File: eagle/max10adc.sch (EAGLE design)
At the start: 203 parts, among them IC1 MAX19506, IC2 MAX19506, J1 MOLEX_BNC_73100-0105, J2 MOLEX_BNC_73100-0105, J3 MOLEX_BNC_73100-0105, J4 MOLEX_BNC_73100-0105, K1 AQY21SOP, K2 AQY21SOP, K3 AQY21SOP, K4 AQY21SOP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

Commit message: for 8.7 and USB2
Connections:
- net +3V3: no longer PIN_DISPLAY.2
- net +5V: now also PIN_DISPLAY.2
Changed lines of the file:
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@@
 <part name="USB1" library="PP_Connectors" deviceset="USB_5PIN" device="_10118193-0001LF" value="MF-CON-MICROUSB-RIGHT"/>
 <part name="GND42" library="supply1" deviceset="GND" device=""/>
-<part name="+3V22" library="supply1" deviceset="+3V3" device=""/>
 <part name="SW_RESET" library="MF_Switches" deviceset="TACT" device="_4.2MM" value="MF-SW-TACT-4.2MM"/>
 <part name="+3V16" library="supply1" deviceset="+3V3" device=""/>
@@
 <attribute name="MPN" value="MF-CAP-0805-1uF"/>
 </part>
+<part name="P+6" library="supply1" deviceset="+5V" device=""/>
 </parts>
 <sheets>
@@
 <instance part="USB1" gate="G$1" x="-375.92" y="-104.14"/>
 <instance part="GND42" gate="1" x="-480.06" y="78.994"/>
-<instance part="+3V22" gate="G$1" x="-474.98" y="68.58" smashed="yes" rot="R180">
-<attribute name="VALUE" x="-474.98" y="72.39" size="1.778" layer="96" rot="R90"/>
-</instance>
 <instance part="SW_RESET" gate="G$1" x="-431.8" y="86.36" smashed="yes">
 <attribute name="NAME" x="-434.34" y="86.36" size="1.016" layer="95" font="vector" align="top-left"/>
@@
 <attribute name="NAME" x="-461.01" y="111.76" size="1.27" layer="95" ratio="10" rot="R180"/>
 </instance>
-<instance part="P+7" gate="1" x="-474.98" y="121.92"/>
-<instance part="GND68" gate="1" x="-477.52" y="114.3" rot="R180"/>
+<instance part="P+7" gate="1" x="-480.06" y="96.52" rot="R90"/>
+<instance part="GND68" gate="1" x="-480.06" y="101.6"/>
 <instance part="GND69" gate="1" x="-355.6" y="-116.84" rot="R90"/>
 <instance part="K1" gate="G$1" x="-228.6" y="-104.14" rot="R180"/>
@@
 <attribute name="MPN" x="-596.9" y="-60.96" size="1.778" layer="96" display="off"/>
 </instance>
+<instance part="P+6" gate="1" x="-480.06" y="73.66" rot="R90"/>
 </instances>
 <busses>
@@
 <pinref part="PIN_IO_1" gate="G$1" pin="2"/>
 <pinref part="P+7" gate="1" pin="+5V"/>
-<wire x1="-474.98" y1="119.38" x2="-474.98" y2="104.14" width="0.1524" layer="91"/>
+<wire x1="-477.52" y1="96.52" x2="-474.98" y2="104.14" width="0.1524" layer="91"/>
 </segment>
 <segment>
@@
 <pinref part="P+4" gate="1" pin="+5V"/>
 <wire x1="-337.82" y1="-127" x2="-337.82" y2="-121.92" width="0.1524" layer="91"/>
+</segment>
+<segment>
+<pinref part="PIN_DISPLAY" gate="G$1" pin="2"/>
+<wire x1="-477.52" y1="73.66" x2="-474.98" y2="81.534" width="0.1524" layer="91"/>
+<pinref part="P+6" gate="1" pin="+5V"/>
 </segment>
 </net>
@@
 <pinref part="PIN_IO_1" gate="G$1" pin="1"/>
 <pinref part="GND68" gate="1" pin="GND"/>
-<wire x1="-477.52" y1="111.76" x2="-477.52" y2="104.14" width="0.1524" layer="91"/>
+<wire x1="-480.06" y1="104.14" x2="-477.52" y2="104.14" width="0.1524" layer="91"/>
 </segment>
 <segment>
@@
 <junction x="-393.7" y="-142.24"/>
 </segment>
-<segment>
-<pinref part="+3V22" gate="G$1" pin="+3V3"/>
-<pinref part="PIN_DISPLAY" gate="G$1" pin="2"/>
-<wire x1="-474.98" y1="71.12" x2="-474.98" y2="81.534" width="0.1524" layer="91"/>
-</segment>
 </net>

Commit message: for 8.7 use 1210 10uF caps for offset
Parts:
- removed COFFSETB11, COFFSETB5, COFFSETB7, COFFSETB9: 10uF, rcl:C-EUC0805K
- added COFFSETA1, COFFSETA2, COFFSETA3, COFFSETA6: 10uF, rcl@1:C-USC1206
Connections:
- net GND: now also COFFSETA1.1, COFFSETA2.1, COFFSETA3.1, COFFSETA6.1; no longer COFFSETB11.1, COFFSETB5.1, COFFSETB7.1, COFFSETB9.1
- net OFFSET1: now also COFFSETA6.2; no longer COFFSETB5.2
- net OFFSET2: now also COFFSETA1.2; no longer COFFSETB7.2
- net OFFSET3: now also COFFSETA2.2; no longer COFFSETB9.2
- net OFFSET4: now also COFFSETA3.2; no longer COFFSETB11.2
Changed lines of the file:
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@@
 <part name="GND60" library="supply1" deviceset="GND" device=""/>
 <part name="GND61" library="supply1" deviceset="GND" device=""/>
-<part name="COFFSETB5" library="rcl" deviceset="C-EU" device="C0805K" value="10uF">
-<attribute name="MPN" value="MF-CAP-0805-10uF"/>
-</part>
 <part name="COFFSETB6" library="rcl" deviceset="C-EU" device="C0805K" value="0.1uF">
 <attribute name="MPN" value="MF-CAP-0805-0.1uF"/>
 </part>
 <part name="GND58" library="supply1" deviceset="GND" device=""/>
-<part name="COFFSETB7" library="rcl" deviceset="C-EU" device="C0805K" value="10uF">
-<attribute name="MPN" value="MF-CAP-0805-10uF"/>
-</part>
 <part name="COFFSETB8" library="rcl" deviceset="C-EU" device="C0805K" value="0.1uF">
 <attribute name="MPN" value="MF-CAP-0805-0.1uF"/>
 </part>
 <part name="GND59" library="supply1" deviceset="GND" device=""/>
-<part name="COFFSETB9" library="rcl" deviceset="C-EU" device="C0805K" value="10uF">
-<attribute name="MPN" value="MF-CAP-0805-10uF"/>
-</part>
 <part name="COFFSETB10" library="rcl" deviceset="C-EU" device="C0805K" value="0.1uF">
 <attribute name="MPN" value="MF-CAP-0805-0.1uF"/>
 </part>
 <part name="GND62" library="supply1" deviceset="GND" device=""/>
-<part name="COFFSETB11" library="rcl" deviceset="C-EU" device="C0805K" value="10uF">
-<attribute name="MPN" value="MF-CAP-0805-10uF"/>
-</part>
 <part name="COFFSETB12" library="rcl" deviceset="C-EU" device="C0805K" value="0.1uF">
 <attribute name="MPN" value="MF-CAP-0805-0.1uF"/>
@@
 </part>
 <part name="P+6" library="supply1" deviceset="+5V" device=""/>
+<part name="COFFSETA6" library="rcl@1" deviceset="C-US" device="C1206" value="10uF">
+<attribute name="MPN" value="MF-CAP-1206-10uF"/>
+</part>
+<part name="COFFSETA1" library="rcl@1" deviceset="C-US" device="C1206" value="10uF">
+<attribute name="MPN" value="MF-CAP-1206-10uF"/>
+</part>
+<part name="COFFSETA2" library="rcl@1" deviceset="C-US" device="C1206" value="10uF">
+<attribute name="MPN" value="MF-CAP-1206-10uF"/>
+</part>
+<part name="COFFSETA3" library="rcl@1" deviceset="C-US" device="C1206" value="10uF">
+<attribute name="MPN" value="MF-CAP-1206-10uF"/>
+</part>
 </parts>
 <sheets>
@@
 <instance part="GND60" gate="1" x="-96.52" y="30.48"/>
 <instance part="GND61" gate="1" x="-96.52" y="53.34"/>
-<instance part="COFFSETB5" gate="G$1" x="-254" y="-215.9" smashed="yes" rot="R180">
-<attribute name="MPN" x="-254" y="-215.9" size="1.778" layer="96" rot="R180" display="off"/>
-<attribute name="NAME" x="-250.444" y="-221.361" size="1.778" layer="95" rot="R180"/>
-<attribute name="VALUE" x="-255.524" y="-211.201" size="1.778" layer="96" rot="R180"/>
-</instance>
 <instance part="COFFSETB6" gate="G$1" x="-261.62" y="-215.9" smashed="yes" rot="R180">
 <attribute name="MPN" x="-261.62" y="-215.9" size="1.778" layer="96" rot="R180" display="off"/>
@@
 </instance>
 <instance part="GND58" gate="1" x="-254" y="-223.52"/>
-<instance part="COFFSETB7" gate="G$1" x="-182.88" y="-218.44" smashed="yes" rot="R180">
-<attribute name="MPN" x="-182.88" y="-218.44" size="1.778" layer="96" rot="R180" display="off"/>
-<attribute name="NAME" x="-179.324" y="-223.901" size="1.778" layer="95" rot="R180"/>
-<attribute name="VALUE" x="-184.404" y="-213.741" size="1.778" layer="96" rot="R180"/>
-</instance>
 <instance part="COFFSETB8" gate="G$1" x="-190.5" y="-218.44" smashed="yes" rot="R180">
 <attribute name="MPN" x="-190.5" y="-218.44" size="1.778" layer="96" rot="R180" display="off"/>
@@
 </instance>
 <instance part="GND59" gate="1" x="-182.88" y="-226.06"/>
-<instance part="COFFSETB9" gate="G$1" x="-170.18" y="-215.9" smashed="yes" rot="R180">
-<attribute name="MPN" x="-170.18" y="-215.9" size="1.778" layer="96" rot="R180" display="off"/>
-<attribute name="NAME" x="-166.624" y="-221.361" size="1.778" layer="95" rot="R180"/>
-<attribute name="VALUE" x="-171.704" y="-211.201" size="1.778" layer="96" rot="R180"/>
-</instance>
 <instance part="COFFSETB10" gate="G$1" x="-177.8" y="-215.9" smashed="yes" rot="R180">
 <attribute name="MPN" x="-177.8" y="-215.9" size="1.778" layer="96" rot="R180" display="off"/>
@@
 </instance>
 <instance part="GND62" gate="1" x="-170.18" y="-223.52"/>
-<instance part="COFFSETB11" gate="G$1" x="-96.52" y="-218.44" smashed="yes" rot="R180">
-<attribute name="MPN" x="-96.52" y="-218.44" size="1.778" layer="96" rot="R180" display="off"/>
-<attribute name="NAME" x="-92.964" y="-223.901" size="1.778" layer="95" rot="R180"/>
-<attribute name="VALUE" x="-98.044" y="-213.741" size="1.778" layer="96" rot="R180"/>
-</instance>
 <instance part="COFFSETB12" gate="G$1" x="-104.14" y="-218.44" smashed="yes" rot="R180">
 <attribute name="MPN" x="-104.14" y="-218.44" size="1.778" layer="96" rot="R180" display="off"/>
@@
 </instance>
 <instance part="P+6" gate="1" x="-480.06" y="73.66" rot="R90"/>
+<instance part="COFFSETA6" gate="G$1" x="-254" y="-215.9" rot="R180">
+<attribute name="MPN" x="-254" y="-215.9" size="1.778" layer="96" rot="R180" display="off"/>
+</instance>
+<instance part="COFFSETA1" gate="G$1" x="-182.88" y="-218.44" rot="R180">
+<attribute name="MPN" x="-182.88" y="-218.44" size="1.778" layer="96" rot="R180" display="off"/>
+</instance>
+<instance part="COFFSETA2" gate="G$1" x="-170.18" y="-215.9" rot="R180">
+<attribute name="MPN" x="-170.18" y="-215.9" size="1.778" layer="96" rot="R180" display="off"/>
+</instance>
+<instance part="COFFSETA3" gate="G$1" x="-96.52" y="-218.44" rot="R180">
+<attribute name="MPN" x="-96.52" y="-218.44" size="1.778" layer="96" rot="R180" display="off"/>
+</instance>
 </instances>
 <busses>
@@
 </segment>
 <segment>
-<pinref part="COFFSETB5" gate="G$1" pin="1"/>
 <pinref part="GND58" gate="1" pin="GND"/>
 <wire x1="-254" y1="-220.98" x2="-254" y2="-218.44" width="0.1524" layer="91"/>
 <pinref part="COFFSETB6" gate="G$1" pin="1"/>
 <wire x1="-261.62" y1="-218.44" x2="-254" y2="-218.44" width="0.1524" layer="91"/>
+<pinref part="COFFSETA6" gate="G$1" pin="1"/>
 <junction x="-254" y="-218.44"/>
 </segment>
 <segment>
-<pinref part="COFFSETB7" gate="G$1" pin="1"/>
 <pinref part="GND59" gate="1" pin="GND"/>
 <wire x1="-182.88" y1="-223.52" x2="-182.88" y2="-220.98" width="0.1524" layer="91"/>
 <pinref part="COFFSETB8" gate="G$1" pin="1"/>
 <wire x1="-190.5" y1="-220.98" x2="-182.88" y2="-220.98" width="0.1524" layer="91"/>
+<pinref part="COFFSETA1" gate="G$1" pin="1"/>
 <junction x="-182.88" y="-220.98"/>
 </segment>
 <segment>
-<pinref part="COFFSETB9" gate="G$1" pin="1"/>
 <pinref part="GND62" gate="1" pin="GND"/>
 <wire x1="-170.18" y1="-220.98" x2="-170.18" y2="-218.44" width="0.1524" layer="91"/>
 <pinref part="COFFSETB10" gate="G$1" pin="1"/>
 <wire x1="-177.8" y1="-218.44" x2="-170.18" y2="-218.44" width="0.1524" layer="91"/>
+<pinref part="COFFSETA2" gate="G$1" pin="1"/>
 <junction x="-170.18" y="-218.44"/>
 </segment>
 <segment>
-<pinref part="COFFSETB11" gate="G$1" pin="1"/>
 <pinref part="GND63" gate="1" pin="GND"/>
 <wire x1="-96.52" y1="-223.52" x2="-96.52" y2="-220.98" width="0.1524" layer="91"/>
 <pinref part="COFFSETB12" gate="G$1" pin="1"/>
 <wire x1="-104.14" y1="-220.98" x2="-96.52" y2="-220.98" width="0.1524" layer="91"/>
+<pinref part="COFFSETA3" gate="G$1" pin="1"/>
 <junction x="-96.52" y="-220.98"/>
 </segment>
@@
 <net name="OFFSET1" class="0">
 <segment>
-<wire x1="-246.38" y1="-210.82" x2="-254" y2="-210.82" width="0.1524" layer="91"/>
 <label x="-264.16" y="-210.82" size="1.778" layer="95"/>
 <pinref part="U1" gate="A" pin="+INA"/>
-<pinref part="COFFSETB5" gate="G$1" pin="2"/>
-<wire x1="-254" y1="-210.82" x2="-261.62" y2="-210.82" width="0.1524" layer="91"/>
-<junction x="-254" y="-210.82"/>
+<wire x1="-246.38" y1="-210.82" x2="-254" y2="-210.82" width="0.1524" layer="91"/>
 <pinref part="COFFSETB6" gate="G$1" pin="2"/>
 <junction x="-261.62" y="-210.82"/>
+<wire x1="-254" y1="-210.82" x2="-261.62" y2="-210.82" width="0.1524" layer="91"/>
 <wire x1="-261.62" y1="-210.82" x2="-264.16" y2="-210.82" width="0.1524" layer="91"/>
+<pinref part="COFFSETA6" gate="G$1" pin="2"/>
+<junction x="-254" y="-210.82"/>
 </segment>
 <segment>
@@
 <wire x1="-190.5" y1="-213.36" x2="-182.88" y2="-213.36" width="0.1524" layer="91"/>
 <label x="-193.04" y="-213.36" size="1.778" layer="95"/>
-<pinref part="COFFSETB7" gate="G$1" pin="2"/>
 <pinref part="COFFSETB8" gate="G$1" pin="2"/>
 <junction x="-190.5" y="-213.36"/>
-<junction x="-182.88" y="-213.36"/>
+<pinref part="COFFSETA1" gate="G$1" pin="2"/>
 <wire x1="-182.88" y1="-213.36" x2="-180.34" y2="-213.36" width="0.1524" layer="91"/>
+<junction x="-182.88" y="-213.36"/>
 </segment>
 <segment>
@@
 <segment>
 <pinref part="U2" gate="A" pin="+INA"/>
-<wire x1="-165.1" y1="-210.82" x2="-170.18" y2="-210.82" width="0.1524" layer="91"/>
 <label x="-182.88" y="-210.82" size="1.778" layer="95"/>
 <pinref part="COFFSETB10" gate="G$1" pin="2"/>
 <junction x="-177.8" y="-210.82"/>
+<wire x1="-165.1" y1="-210.82" x2="-170.18" y2="-210.82" width="0.1524" layer="91"/>
 <wire x1="-170.18" y1="-210.82" x2="-177.8" y2="-210.82" width="0.1524" layer="91"/>
 <wire x1="-177.8" y1="-210.82" x2="-182.88" y2="-210.82" width="0.1524" layer="91"/>
-<pinref part="COFFSETB9" gate="G$1" pin="2"/>
+<pinref part="COFFSETA2" gate="G$1" pin="2"/>
 <junction x="-170.18" y="-210.82"/>
 </segment>
@@
 <junction x="-104.14" y="-213.36"/>
 <wire x1="-104.14" y1="-213.36" x2="-96.52" y2="-213.36" width="0.1524" layer="91"/>
-<pinref part="COFFSETB11" gate="G$1" pin="2"/>
-<junction x="-96.52" y="-213.36"/>
+<pinref part="COFFSETA3" gate="G$1" pin="2"/>
 <wire x1="-96.52" y1="-213.36" x2="-93.98" y2="-213.36" width="0.1524" layer="91"/>
+<junction x="-96.52" y="-213.36"/>
 </segment>
 <segment>

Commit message: v8.7 just ordered from AllPCB
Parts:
- removed CIN1, CIN2, CIN3, CIN4: 10pF, rcl@1:C-USC0603
- removed CIN56_5, CIN56_6, CIN56_7, CIN56_8: 56pF, rcl@1:C-USC0603
- removed HGR1, HGR2, HGR3, HGR4: 560, resistor:R-EU_R0805
- removed K5, K6, K7, K8: AQY21SOP, relay:AQY21SOP
- added C1, C2, C3, C4: 3-10pF, SparkFun-Passives:CAP_ADJSMD
- added CIN5_1, CIN5_2, CIN5_3, CIN5_4: 5pF, rcl@1:C-USC0603
- added C_S1, C_S2, C_S3, C_S4: 8-45pF, SparkFun-Passives:CAP_ADJSMD
- added LEDPOW: MF-LED-0805-RED, led:LEDSML0805
- added RIN5, RIN6, RIN7, RIN8: 1M, resistor:R-EU_R0805
- added RLEDPOW: 560, resistor:R-EU_R0805
- added SW_SUPER1, SW_SUPER2, SW_SUPER3, SW_SUPER4: 0S102011MS2QS1, PP_Electromechanical:SPDT_0S102011MS2QS1
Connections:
- removed net E_20_B7: IOEXPAND_0X20_BOT.GPB7, PIN_AIN_IO2_PWRGND.2
- removed net E_HIGHGAIN1: HGR1.1, IOEXPAND_0X20_BOT.GPA4
- removed net E_HIGHGAIN2: HGR2.1, IOEXPAND_0X20_BOT.GPA5
- removed net E_HIGHGAIN3: HGR3.1, IOEXPAND_0X20_BOT.GPA6
- removed net E_HIGHGAIN4: HGR4.1, IOEXPAND_0X20_BOT.GPA7
- removed net E_SHDN: IC1.SHDN, IC2.SHDN, IOEXPAND_0X20_BOT.GPB4
- removed net N$36: HGR2.2, K6.A
- removed net N$37: HGR3.2, K7.A
- removed net N$43: HGR4.2, K8.A
- new net E_SHDN1: IC1.SHDN, IOEXPAND_0X20_BOT.GPB4
- new net E_SHDN2: IC2.SHDN, IOEXPAND_0X20_BOT.GPB5
- net +3V3: now also LEDPOW.A, PIN_AIN_IO2_PWRGND.3
- net AIN1: now also PIN_AIN_IO2_PWRGND.2; no longer PIN_AIN_IO2_PWRGND.1
- net E_OVSAMP1: now also IOEXPAND_0X20_BOT.GPA4; no longer IOEXPAND_0X20_BOT.GPB5
- net E_OVSAMP2: now also IOEXPAND_0X20_BOT.GPA5; no longer IOEXPAND_0X20_BOT.GPB6
- net GND: now also PIN_AIN_IO2_PWRGND.1, RIN5.2, RIN6.2, RIN7.2, RIN8.2, RLEDPOW.2; no longer K5.K, K6.K, K7.K, K8.K, PIN_AIN_IO2_PWRGND.4
- net INAMINUS1: now also C1.4, CIN5_1.1, C_S1.4; no longer CIN1.2, CIN56_2.2
- net INAMINUS2: now also C3.4, CIN56_3.2, CIN5_3.1, C_S3.4; no longer CIN3.2, CIN56_5.2, CIN56_6.2
- net INBMINUS1: now also C2.4, CIN56_2.2, CIN5_2.1, C_S2.4; no longer CIN2.2, CIN56_3.2, CIN56_4.2
- net INBMINUS2: now also C4.4, CIN56_4.2, CIN5_4.1, C_S4.4; no longer CIN4.2, CIN56_7.2, CIN56_8.2
- net IO_100: now also PIN_AIN_IO2_PWRGND.13; no longer PIN_AIN_IO2_PWRGND.11
- net IO_101: now also PIN_AIN_IO2_PWRGND.15; no longer PIN_AIN_IO2_PWRGND.13
- net IO_CLK_88: now also PIN_AIN_IO2_PWRGND.5; no longer PIN_AIN_IO2_PWRGND.3
- net IO_CLK_89: now also PIN_AIN_IO2_PWRGND.7; no longer PIN_AIN_IO2_PWRGND.5
- net IO_CLK_90: now also PIN_AIN_IO2_PWRGND.9; no longer PIN_AIN_IO2_PWRGND.7
- net IO_CLK_91: now also PIN_AIN_IO2_PWRGND.11; no longer PIN_AIN_IO2_PWRGND.9
- net L121: now also PIN_AIN_IO2_PWRGND.4; no longer PIN_AIN_IO2_PWRGND.15
- net N$10: now also C1.3, CIN5_1.2, RIN5.1, SW_SUPER1.C; no longer CIN1.1, K5.DS2
- net N$15: now also C2.3, CIN5_2.2, RIN6.1, SW_SUPER2.C; no longer CIN2.1, K6.DS2
- net N$20: now also C_S1.3, SW_SUPER1.2; no longer CIN56_2.1, K5.DS1
- net N$34: now also LEDPOW.C, RLEDPOW.1; no longer HGR1.2, K5.A
- net N$38: now also CIN56_2.1, C_S2.3, SW_SUPER2.2; no longer CIN56_3.1, CIN56_4.1, K6.DS1
- net N$39: now also C3.3, CIN5_3.2, RIN7.1, SW_SUPER3.C; no longer CIN3.1, K7.DS2
- net N$40: now also CIN56_3.1, C_S3.3, SW_SUPER3.2; no longer CIN56_5.1, CIN56_6.1, K7.DS1
- net N$41: now also C4.3, CIN5_4.2, RIN8.1, SW_SUPER4.C; no longer CIN4.1, K8.DS2
- net N$42: now also CIN56_4.1, C_S4.3, SW_SUPER4.2; no longer CIN56_7.1, CIN56_8.1, K8.DS1
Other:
- moved on the sheet: CIN56_2, CIN56_3, CIN56_4

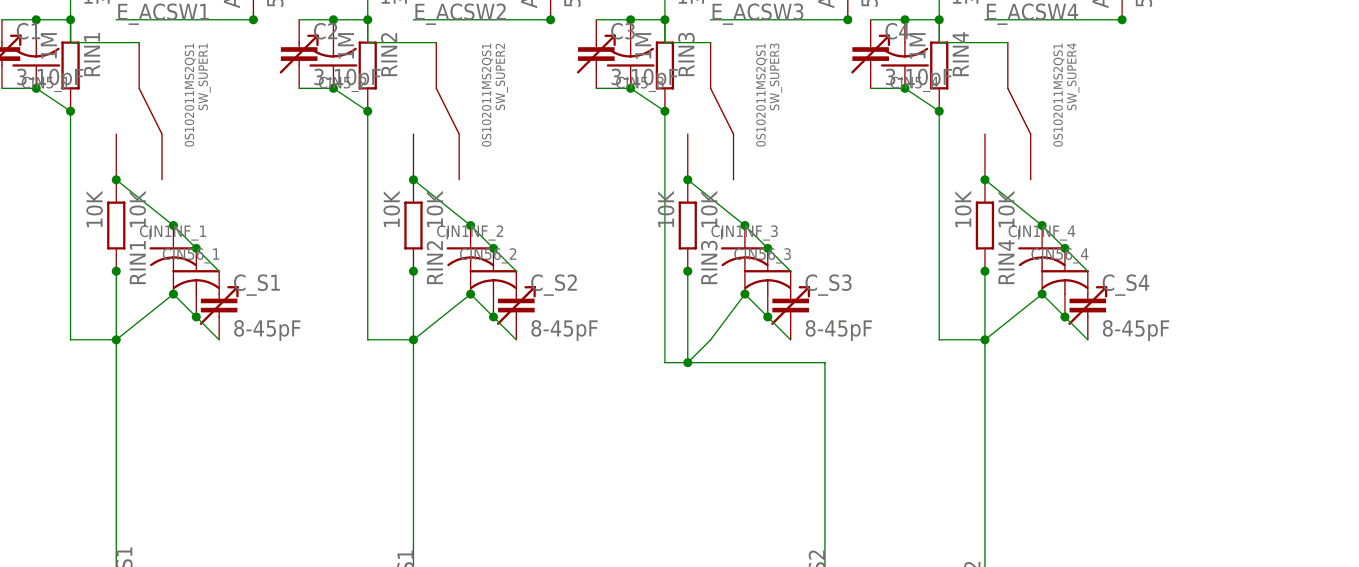
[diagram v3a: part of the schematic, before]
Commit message: v8.8 with 50pF low gain caps
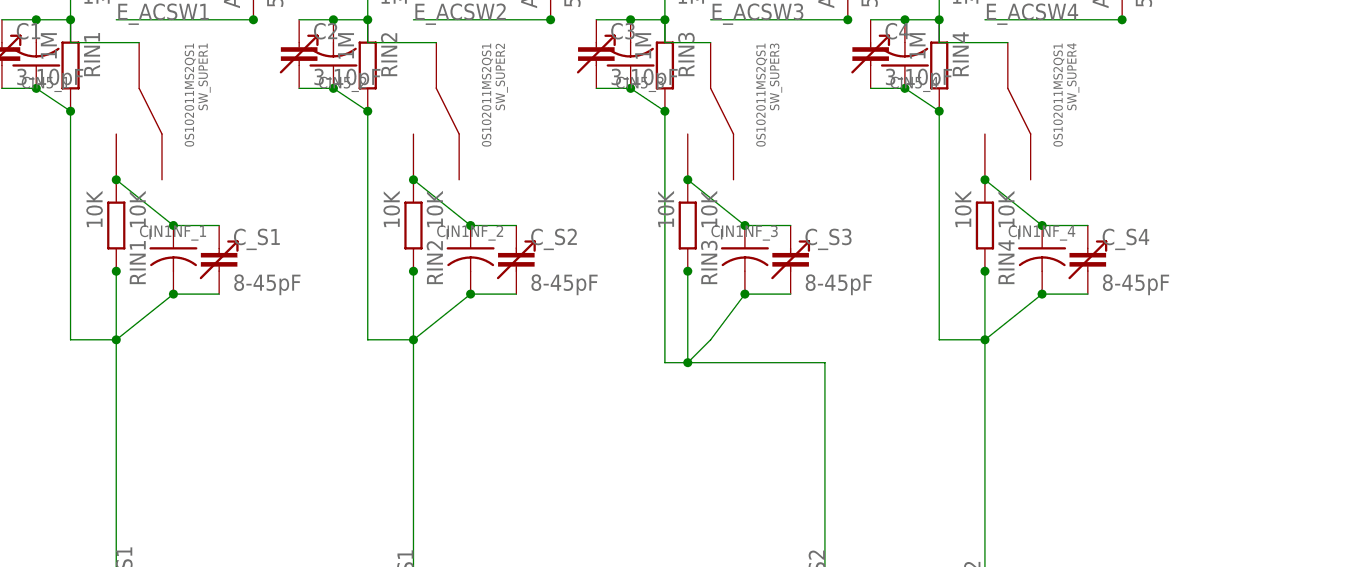
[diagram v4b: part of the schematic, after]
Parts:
- removed CIN56_1, CIN56_2, CIN56_3, CIN56_4: 56pF, rcl@1:C-USC0603
- CGAIN1_1, CGAIN1_2, CGAIN1_3, CGAIN1_4: value 56pF -> 50pF; MPN 06035A560FAT2A -> 06035A500JAT2A
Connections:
- net INAMINUS1: no longer CIN56_1.2
- net INAMINUS2: no longer CIN56_3.2
- net INBMINUS1: no longer CIN56_2.2
- net INBMINUS2: no longer CIN56_4.2
- net N$20: no longer CIN56_1.1
- net N$38: no longer CIN56_2.1
- net N$40: no longer CIN56_3.1
- net N$42: no longer CIN56_4.1
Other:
- moved on the sheet: C_S1, C_S2, C_S3, C_S4

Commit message: v8.8
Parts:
- removed C1, C2, C3, C4: 3-10pF, SparkFun-Passives:CAP_ADJSMD
- removed CGAIN2_1, CGAIN2_2, CGAIN2_3, CGAIN2_4: 5pF, rcl@1:C-USC0603
- removed C_S1, C_S2, C_S3, C_S4: 8-45pF, SparkFun-Passives:CAP_ADJSMD
- added CH1, CH2, CH3, CH4: 3-10pF, SparkFun-Passives:CAP_ADJSMD
- added CIN56_1, CIN56_2, CIN56_3, CIN56_4: 56pF, rcl@1:C-USC0603
- added CL1, CL2, CL3, CL4: 8-45pF, SparkFun-Passives:CAP_ADJSMD
- CGAIN1_1, CGAIN1_2, CGAIN1_3, CGAIN1_4: value 50pF -> 33pF; MPN 06035A500JAT2A -> 06033A330JAT2A
- CIN1NF_1, CIN1NF_2, CIN1NF_3, CIN1NF_4: MFN MF-CAP-0603-1nF -> (none); MPN (none) -> 06035A102JAT2A
- CIN5_1, CIN5_2, CIN5_3, CIN5_4: value 5pF -> 10pF; MPN C1608C0G1H050C080AA -> MF-CAP-0603-10pF
- R_SCL, R_SDA: value 4.7k -> 10K; MPN MF-RES-0805-4.7K -> MF-RES-0805-10K
- SW_5V, SW_SUPER1, SW_SUPER2, SW_SUPER3, SW_SUPER4, SW_TERM1, SW_TERM2, SW_TERM3, SW_TERM4: value 0S102011MS2QS1 -> OS102011MS2QN1
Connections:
- removed net N$42: CIN1NF_4.1, C_S4.3, RIN4_10K.1, SW_SUPER4.2
- new net N$36: CIN1NF_4.1, CIN56_4.1, RIN4_10K.1, SW_SUPER4.2
- net CGAIN1: now also CL1.4
- net CGAIN2: now also CH1.4; no longer CGAIN2_1.2
- net CGAIN3: now also CL2.4
- net CGAIN4: now also CH2.4; no longer CGAIN2_2.2
- net CGAIN5: now also CL3.4
- net CGAIN6: now also CH3.4; no longer CGAIN2_3.2
- net CGAIN7: now also CL4.4
- net CGAIN8: now also CH4.4; no longer CGAIN2_4.2
- net INAMINUS1: now also CH1.3, CIN56_1.2, CL1.3; no longer C1.4, CGAIN2_1.1, C_S1.4
- net INAMINUS2: now also CH3.3, CIN56_3.2, CL3.3; no longer C3.4, CGAIN2_3.1, C_S3.4
- net INBMINUS1: now also CH2.3, CIN56_2.2, CL2.3; no longer C2.4, CGAIN2_2.1, C_S2.4
- net INBMINUS2: now also CH4.3, CIN56_4.2, CL4.3; no longer C4.4, CGAIN2_4.1, C_S4.4
- net N$10: no longer C1.3
- net N$15: no longer C2.3
- net N$20: now also CIN56_1.1; no longer C_S1.3
- net N$38: now also CIN56_2.1; no longer C_S2.3
- net N$39: no longer C3.3
- net N$40: now also CIN56_3.1; no longer C_S3.3
- net N$41: no longer C4.3
